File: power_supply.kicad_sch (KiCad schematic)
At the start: 37 parts, among them CON1 USB_B_Micro, CON2 Barrel_Jack_MountingPin, Q1 AO3401A, U1 AP1117-33, U2 AP6503, U3 CP2102N

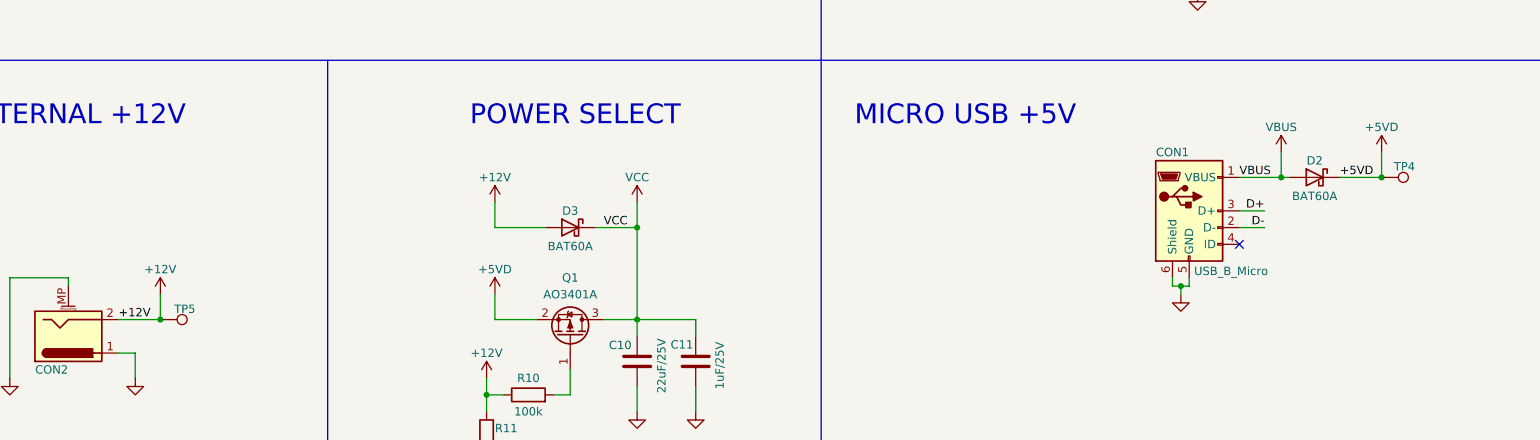
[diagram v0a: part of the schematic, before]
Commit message: Corrigido hierarchical label +3.3V do Módulo IoT
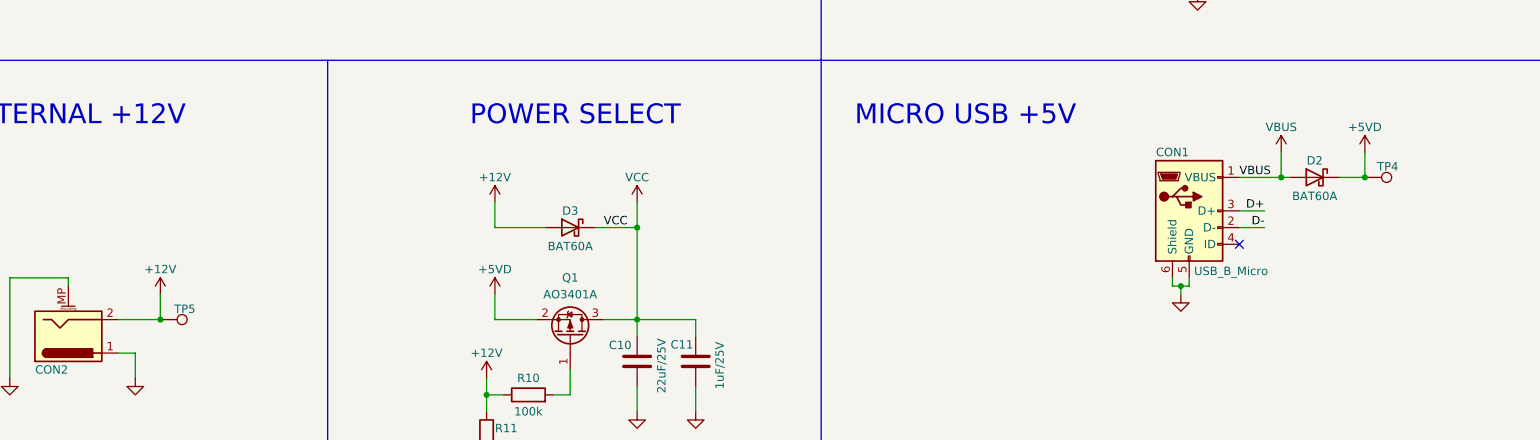
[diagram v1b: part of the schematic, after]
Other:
- moved on the sheet: TP4
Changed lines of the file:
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@@
   (junction (at 24.13 45.72) (diameter 0) (color 0 0 0 0)
   )
-  (junction (at 245.11 139.7) (diameter 0) (color 0 0 0 0)
+  (junction (at 242.57 139.7) (diameter 0) (color 0 0 0 0)
   )
   (junction (at 139.7 53.34) (diameter 0) (color 0 0 0 0)
@@
     (stroke (width 0) (type default) (color 0 0 0 0))
   )
-  (wire (pts (xy 245.11 135.89) (xy 245.11 139.7))
+  (wire (pts (xy 242.57 135.89) (xy 242.57 139.7))
     (stroke (width 0) (type default) (color 0 0 0 0))
   )
@@
     (stroke (width 0) (type default) (color 0 0 0 0))
   )
-  (wire (pts (xy 238.76 139.7) (xy 245.11 139.7))
+  (wire (pts (xy 238.76 139.7) (xy 242.57 139.7))
     (stroke (width 0) (type default) (color 0 0 0 0))
   )
@@
     (effects (font (size 2.9972 2.9972)) (justify left bottom))
   )
-  (label "+5VD" (at 238.76 139.7 0)
-    (effects (font (size 1.27 1.27)) (justify left bottom))
-  )
   (label "D-" (at 227.33 147.32 180)
     (effects (font (size 1.27 1.27)) (justify right bottom))
   )
   (label "D+" (at 198.12 64.77 0)
-    (effects (font (size 1.27 1.27)) (justify left bottom))
-  )
-  (label "+12V" (at 53.34 161.29 0)
     (effects (font (size 1.27 1.27)) (justify left bottom))
   )
@@
     (pin "2")
   )
-  (symbol (lib_id "Connector:TestPoint") (at 245.11 139.7 270) (unit 1)
-    (in_bom yes) (on_board yes)
-    (property "Reference" "TP4" (id 0) (at 246.9705 138.0585 90)
-      (effects (font (size 1.27 1.27)) (justify left))
-    )
-    (property "Value" "TestPoint" (id 1) (at 247.1421 142.24 0)
+  (symbol (lib_id "Connector:TestPoint") (at 242.57 139.7 270) (unit 1)
+    (in_bom yes) (on_board yes)
+    (property "Reference" "TP4" (id 0) (at 244.4305 138.0585 90)
+      (effects (font (size 1.27 1.27)) (justify left))
+    )
+    (property "Value" "TestPoint" (id 1) (at 244.6021 142.24 0)
       (effects (font (size 1.27 1.27)) (justify left) hide)
     )
-    (property "Footprint" "" (id 2) (at 245.11 144.78 0)
-      (effects (font (size 1.27 1.27)) hide)
-    )
-    (property "Datasheet" "~" (id 3) (at 245.11 144.78 0)
+    (property "Footprint" "" (id 2) (at 242.57 144.78 0)
+      (effects (font (size 1.27 1.27)) hide)
+    )
+    (property "Datasheet" "~" (id 3) (at 242.57 144.78 0)
       (effects (font (size 1.27 1.27)) hide)
     )
@@
     (pin "1")
   )
-  (symbol (lib_id "power:+5VD") (at 245.11 135.89 0) (unit 1)
-    (in_bom yes) (on_board yes)
-    (property "Reference" "#PWR034" (id 0) (at 245.11 139.7 0)
-      (effects (font (size 1.27 1.27)) hide)
-    )
-    (property "Value" "+5VD" (id 1) (at 245.11 132.08 0))
-    (property "Footprint" "" (id 2) (at 245.11 135.89 0)
-      (effects (font (size 1.27 1.27)) hide)
-    )
-    (property "Datasheet" "" (id 3) (at 245.11 135.89 0)
-      (effects (font (size 1.27 1.27)) hide)
-    )
+  (symbol (lib_id "power:+5VD") (at 242.57 135.89 0) (unit 1)
+    (in_bom yes) (on_board yes)
+    (property "Reference" "#PWR034" (id 0) (at 242.57 139.7 0)
+      (effects (font (size 1.27 1.27)) hide)
+    )
+    (property "Value" "+5VD" (id 1) (at 242.57 132.08 0))
+    (property "Footprint" "" (id 2) (at 242.57 135.89 0)
+      (effects (font (size 1.27 1.27)) hide)
+    )
+    (property "Datasheet" "" (id 3) (at 242.57 135.89 0)
+      (effects (font (size 1.27 1.27)) hide)
+    )

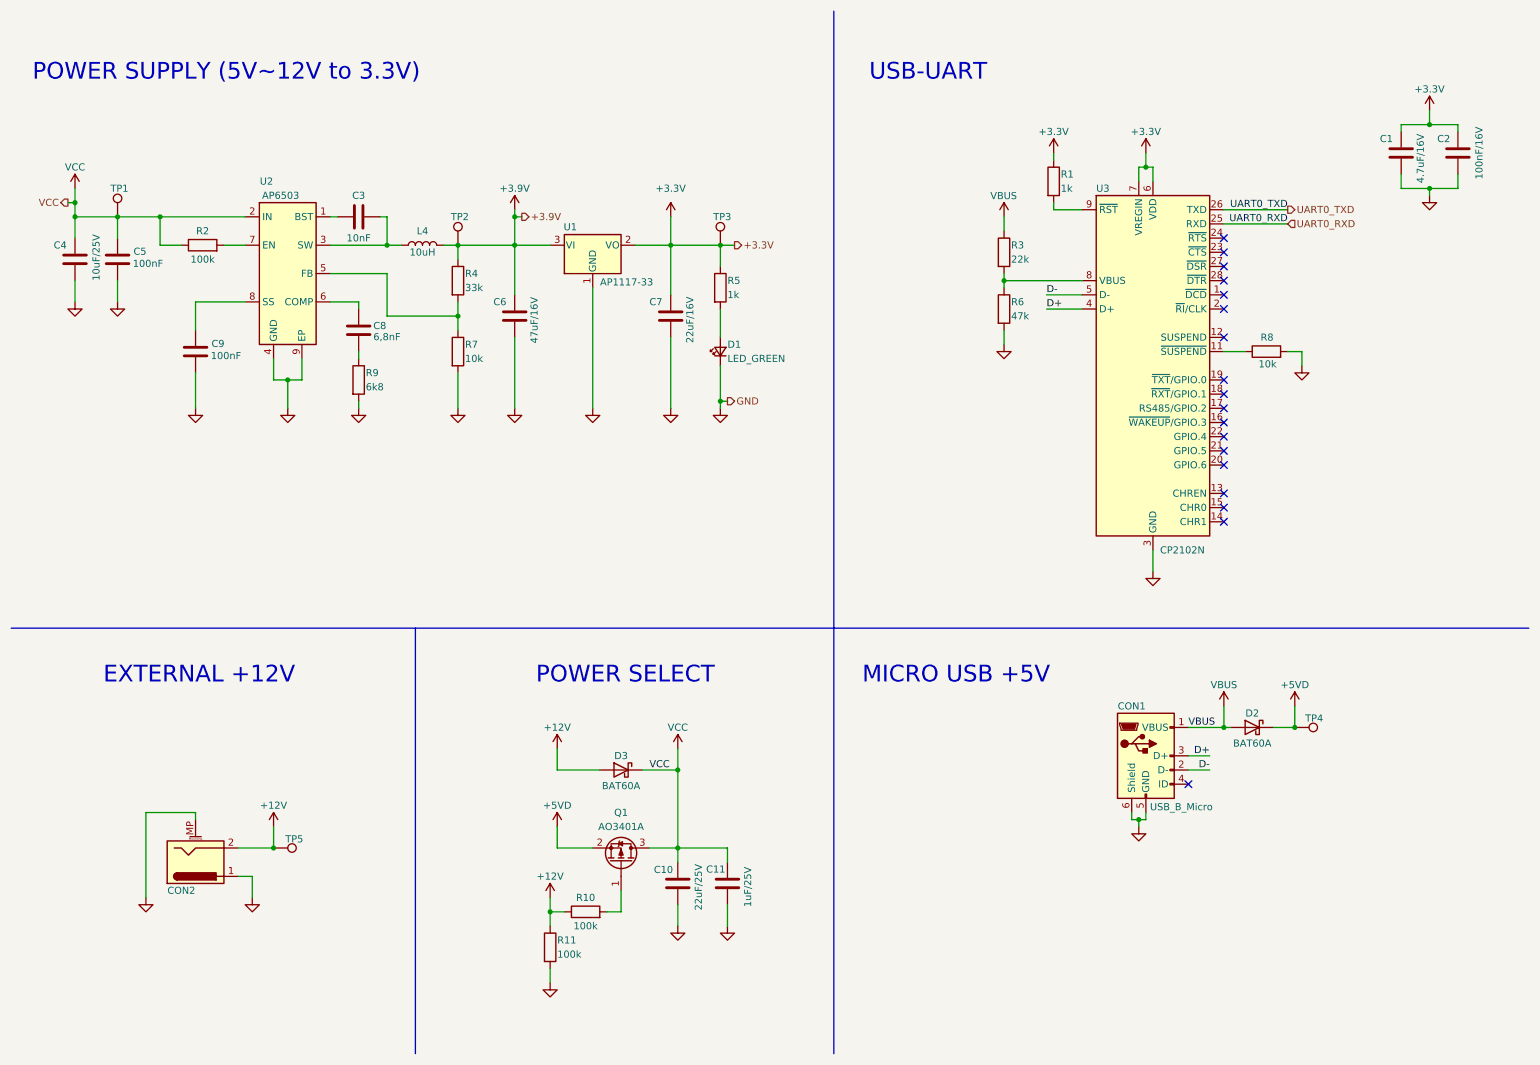
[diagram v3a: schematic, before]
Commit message: Capacitores com encapsulamento 0603
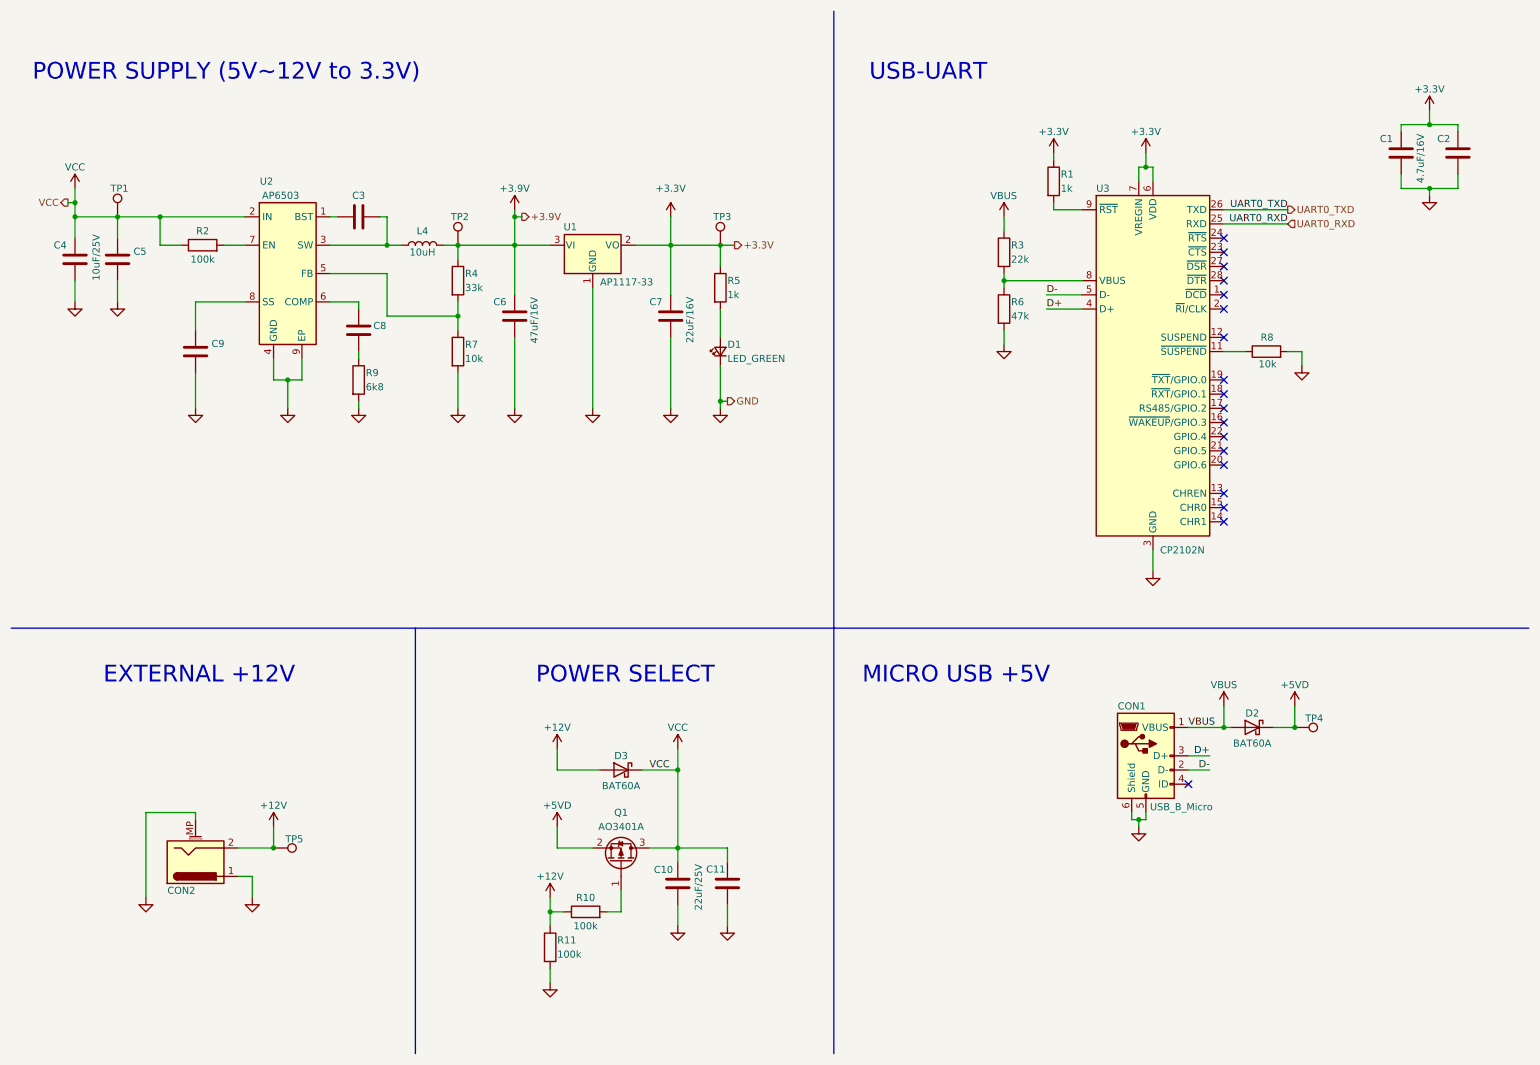
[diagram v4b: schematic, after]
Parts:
- C11: value 1uF/25V -> (none); footprint Capacitor_SMD:C_1206_3216Metric_Pad1.33x1.80mm_HandSolder -> (none)
- C2: value 100nF/16V -> (none); footprint Capacitor_SMD:C_0402_1005Metric_Pad0.74x0.62mm_HandSolder -> (none)
- C3: value 10nF -> (none); footprint Capacitor_SMD:C_0402_1005Metric_Pad0.74x0.62mm_HandSolder -> (none)
- C5, C9: value 100nF -> (none); footprint Capacitor_SMD:C_0402_1005Metric_Pad0.74x0.62mm_HandSolder -> (none)
- C8: value 6,8nF -> (none); footprint Capacitor_SMD:C_0402_1005Metric_Pad0.74x0.62mm_HandSolder -> (none)
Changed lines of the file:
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@@
       (effects (font (size 1.27 1.27)) (justify left))
     )
-    (property "Value" "1uF/25V" (id 1) (at 144.632 171.8591 90)
-      (effects (font (size 1.27 1.27)) (justify left))
-    )
-    (property "Footprint" "Capacitor_SMD:C_1206_3216Metric_Pad1.33x1.80mm_HandSolder" (id 2) (at 141.9352 171.45 0)
+    (property "Value" "" (id 1) (at 144.632 171.8591 90)
+      (effects (font (size 1.27 1.27)) (justify left))
+    )
+    (property "Footprint" "" (id 2) (at 141.9352 171.45 0)
       (effects (font (size 1.27 1.27)) hide)
     )
@@
     (in_bom yes) (on_board yes)
     (property "Reference" "C2" (id 0) (at 269.24 34.29 0))
-    (property "Value" "100nF/16V" (id 1) (at 275.59 36.83 90))
-    (property "Footprint" "Capacitor_SMD:C_0402_1005Metric_Pad0.74x0.62mm_HandSolder" (id 2) (at 270.8148 33.02 0)
+    (property "Value" "" (id 1) (at 275.59 36.83 90))
+    (property "Footprint" "" (id 2) (at 270.8148 33.02 0)
       (effects (font (size 1.27 1.27)) hide)
     )
@@
     (in_bom yes) (on_board yes)
     (property "Reference" "C3" (id 0) (at 74.93 44.45 90))
-    (property "Value" "10nF" (id 1) (at 74.93 52.07 90))
-    (property "Footprint" "Capacitor_SMD:C_0402_1005Metric_Pad0.74x0.62mm_HandSolder" (id 2) (at 78.74 47.2948 0)
+    (property "Value" "" (id 1) (at 74.93 52.07 90))
+    (property "Footprint" "" (id 2) (at 78.74 47.2948 0)
       (effects (font (size 1.27 1.27)) hide)
     )
@@
     (in_bom yes) (on_board yes)
     (property "Reference" "C5" (id 0) (at 35.7705 54.4674 0))
-    (property "Value" "100nF" (id 1) (at 37.2006 56.6367 0))
-    (property "Footprint" "Capacitor_SMD:C_0402_1005Metric_Pad0.74x0.62mm_HandSolder" (id 2) (at 30.7848 52.07 0)
+    (property "Value" "" (id 1) (at 37.2006 56.6367 0))
+    (property "Footprint" "" (id 2) (at 30.7848 52.07 0)
       (effects (font (size 1.27 1.27)) hide)
     )
@@
       (effects (font (size 1.27 1.27)) (justify left))
     )
-    (property "Value" "6,8nF" (id 1) (at 77.5519 69.7652 0)
-      (effects (font (size 1.27 1.27)) (justify left))
-    )
-    (property "Footprint" "Capacitor_SMD:C_0402_1005Metric_Pad0.74x0.62mm_HandSolder" (id 2) (at 75.8952 72.39 0)
+    (property "Value" "" (id 1) (at 77.5519 69.7652 0)
+      (effects (font (size 1.27 1.27)) (justify left))
+    )
+    (property "Footprint" "" (id 2) (at 75.8952 72.39 0)
       (effects (font (size 1.27 1.27)) hide)
     )
@@
     (in_bom yes) (on_board yes)
     (property "Reference" "C9" (id 0) (at 49.7405 70.9774 0))
-    (property "Value" "100nF" (id 1) (at 51.1706 73.1467 0))
-    (property "Footprint" "Capacitor_SMD:C_0402_1005Metric_Pad0.74x0.62mm_HandSolder" (id 2) (at 44.7548 68.58 0)
-      (effects (font (size 1.27 1.27)) hide)
-    )
+    (property "Value" "" (id 1) (at 51.1706 73.1467 0))
+    (property "Footprint" "" (id 2) (at 44.7548 68.58 0)
+      (effects (font (size 1.27 1.27)) hide)
+    )
